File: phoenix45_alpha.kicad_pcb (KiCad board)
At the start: 2 copper layers, 247.7 x 77.5 mm, 114 parts, among them SW1 SW_PUSH, SW2 SW_PUSH, U1 SRV05-4, U3 ATmega32U4-M, X1 Crystal_GND24_Small

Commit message: v1
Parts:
- U3: footprint Package_DFN_QFN:QFN-44-1EP_7x7mm_P0.5mm_EP5.2x5.2mm -> Package_DFN_QFN:QFN-44-1EP_7x7mm_P0.5mm_EP5.2x5.2mm_ThermalVias
- moved D_SPACE13 181.4 mm to (266.6, 38.1), turned to 90 degrees
- moved D_SPACE26 176.1 mm to (266.6, 57.1), turned to 90 degrees
- moved D_SPACE12 147.9 mm to (247.6, 38.1), turned to 90 degrees
- moved D_SPACE47 139.6 mm to (240.4, 95.2), turned to 90 degrees
- moved D_SPACE25 139.5 mm to (247.6, 57.1), turned to 90 degrees
- moved D_SPACE10 137.1 mm to (209.5, 38.1), turned to 90 degrees
- moved D_SPACE1 135.6 mm to (38.0, 38.1), turned to 90 degrees
- moved D_SPACE39 130.1 mm to (261.8, 76.2), turned to 90 degrees
- moved D_SPACE38 127.7 mm to (238.1, 76.2), turned to 90 degrees
- moved D_SPACE11 126.6 mm to (228.5, 38.1), turned to 90 degrees
- moved D_SPACE37 122.8 mm to (219.0, 76.2), turned to 90 degrees
- moved D_SPACE9 119.2 mm to (190.4, 38.1), turned to 90 degrees
- moved D_SPACE2 118.3 mm to (57.1, 38.1), turned to 90 degrees
- moved D_SPACE24 116.1 mm to (228.5, 57.1), turned to 90 degrees
- moved D_SPACE3 114.6 mm to (76.1, 38.1), turned to 90 degrees
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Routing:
- net row0: track 0.00 -> 260.0 mm, vias 0 -> 2
- net row2: track 0.00 -> 254.7 mm
- net row1: track 0.00 -> 237.3 mm, vias 0 -> 3
- net row3: track 0.00 -> 236.3 mm, vias 0 -> 2
- net col0: track 0.00 -> 164.7 mm
- net col12: track 0.00 -> 163.3 mm
- net col1: track 0.00 -> 160.6 mm
- net +5V: track 0.00 -> 159.3 mm, vias 0 -> 7
- net col11: track 0.00 -> 157.7 mm
- net col2: track 0.00 -> 141.1 mm
- net col10: track 0.00 -> 133.7 mm
- net col3: track 0.00 -> 123.6 mm
- net col9: track 0.00 -> 115.4 mm
- net D-: track 0.00 -> 114.5 mm
- net D+: track 0.00 -> 111.8 mm
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
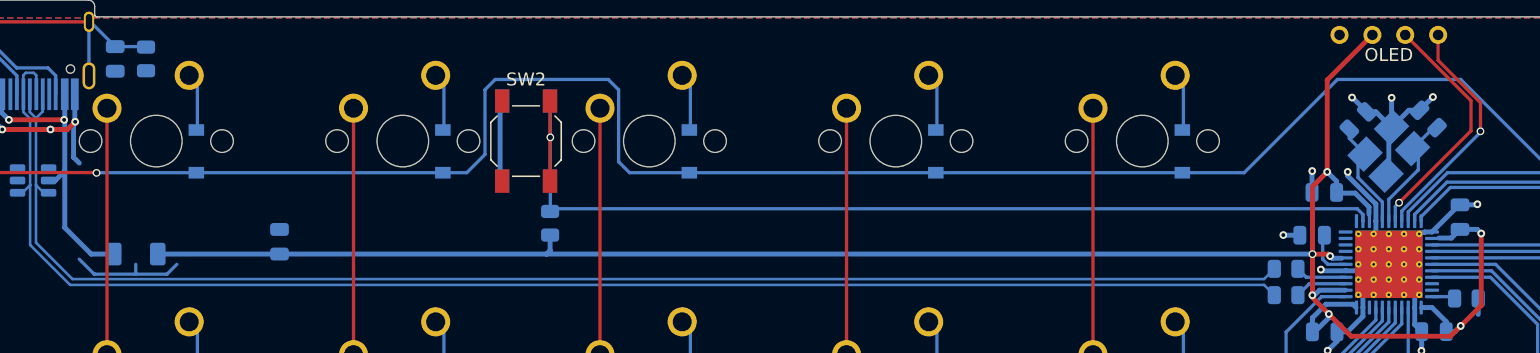
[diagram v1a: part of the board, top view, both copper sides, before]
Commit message: added avr
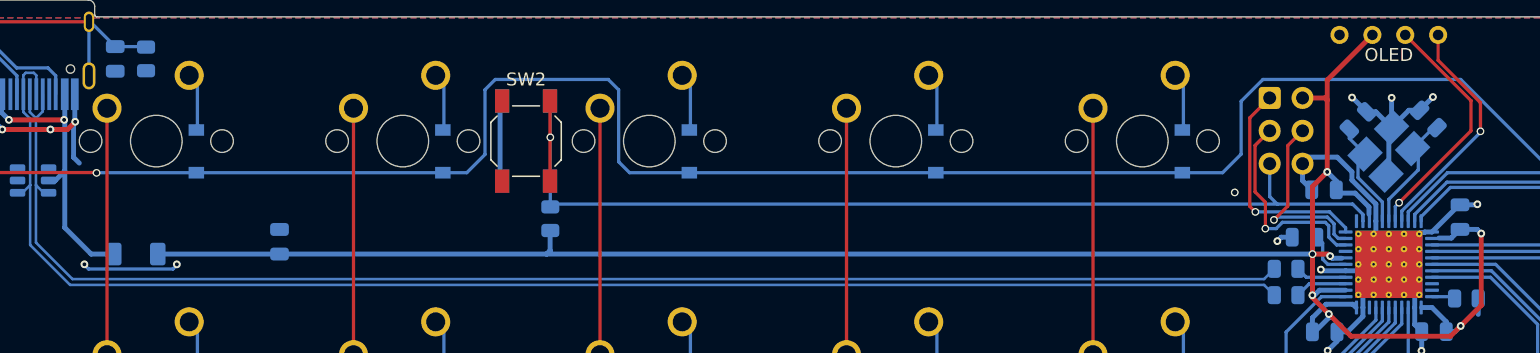
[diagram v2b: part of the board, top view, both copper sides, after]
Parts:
- added J1: AVR-ISP-6, Connector_IDC:IDC-Header_2x03_P2.54mm_Vertical, F.Cu at (140.0, 34.0)
- moved C6 0.61 mm to (142.7, 44.7)
- moved R1 0.35 mm to (84.4, 43.3)
- moved C5 0.20 mm to (144.2, 41.1)
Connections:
- U3 pad 10: unconnected-(U3-Pad10) -> MOSI
- U3 pad 11: unconnected-(U3-Pad11) -> MISO
- U3 pad 9: unconnected-(U3-Pad9) -> SCK
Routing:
- net MISO: track 0.00 -> 17.4 mm, vias 0 -> 1
- net SCK: track 0.00 -> 16.0 mm, vias 0 -> 1
- net MOSI: track 0.00 -> 14.6 mm, vias 0 -> 1
- net GND: track 79.5 -> 83.0 mm, vias 13 -> 14
- net RST: track 77.9 -> 81.0 mm
- net row0: track 260.0 -> 262.5 mm
- net +5V: track 159.3 -> 161.3 mm

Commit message: trackpoint
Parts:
- added C9: 2.2uF, Capacitor_SMD:C_0805_2012Metric_Pad1.18x1.45mm_HandSolder, B.Cu at (164.1, 40.1)
- added TP1: TPCLK, TestPoint:TestPoint_Pad_1.0x1.0mm, B.Cu at (162.6, 44.0)
- added TP2: TPVCC, TestPoint:TestPoint_Pad_1.0x1.0mm, B.Cu at (157.8, 44.0)
- added TP3: TPGND, TestPoint:TestPoint_Pad_1.0x1.0mm, B.Cu at (160.2, 44.0)
- added TP4: TPDATA, TestPoint:TestPoint_Pad_1.0x1.0mm, B.Cu at (167.3, 44.0)
- added TP5: TPRST, TestPoint:TestPoint_Pad_1.0x1.0mm, B.Cu at (165.0, 44.0)
- added UR6: 4.7k, Resistor_SMD:R_0805_2012Metric_Pad1.20x1.40mm_HandSolder, B.Cu at (160.6, 41.0)
- added UR7: 4.7k, Resistor_SMD:R_0805_2012Metric_Pad1.20x1.40mm_HandSolder, B.Cu at (157.7, 41.0)
- added UR8: 100k, Resistor_SMD:R_0805_2012Metric_Pad1.20x1.40mm_HandSolder, B.Cu at (164.1, 42.1)
- C0, C1, C2, C3, C4, C5, C6, C7, C8: footprint Capacitor_SMD:C_0805_2012Metric -> Capacitor_SMD:C_0805_2012Metric_Pad1.18x1.45mm_HandSolder
- R1, R2, UR1, UR2, UR3, UR4, UR5: footprint Resistor_SMD:R_0805_2012Metric -> Resistor_SMD:R_0805_2012Metric_Pad1.20x1.40mm_HandSolder
- U1: footprint Package_TO_SOT_SMD:SOT-23-6 -> Package_TO_SOT_SMD:SOT-23-6_Handsoldering
- moved R2 0.56 mm to (155.4, 50.0)
- moved C6 0.24 mm to (142.5, 44.7)
- moved R1 0.18 mm to (84.4, 43.5)
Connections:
- U3 pad 20: row0 -> PD2
- U3 pad 21: col12 -> row0
- U3 pad 22: col11 -> PD5
- U3 pad 25: col10 -> col12
- U3 pad 26: col9 -> col11
- U3 pad 27: col8 -> col10
- U3 pad 28: col7 -> col9
- U3 pad 29: row2 -> col8
- U3 pad 30: row3 -> col7
- U3 pad 31: encA -> row2
- U3 pad 32: encB -> row3
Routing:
- net PD2: track 0.00 -> 21.8 mm, vias 0 -> 2
- net +5V: track 161.3 -> 174.8 mm, vias 7 -> 9
- net PD5: track 0.00 -> 13.1 mm
- net GND: track 83.0 -> 88.7 mm, vias 14 -> 18
- net col12: track 163.3 -> 158.4 mm
- net col11: track 157.7 -> 153.5 mm
- net Net-(C9-Pad2): track 0.00 -> 3.74 mm
- net row0: track 262.5 -> 264.7 mm
- net MOSI: track 14.6 -> 15.5 mm
- net Net-(C8-Pad1): track 7.84 -> 7.14 mm
- net Net-(R2-Pad2): track 1.61 -> 2.15 mm

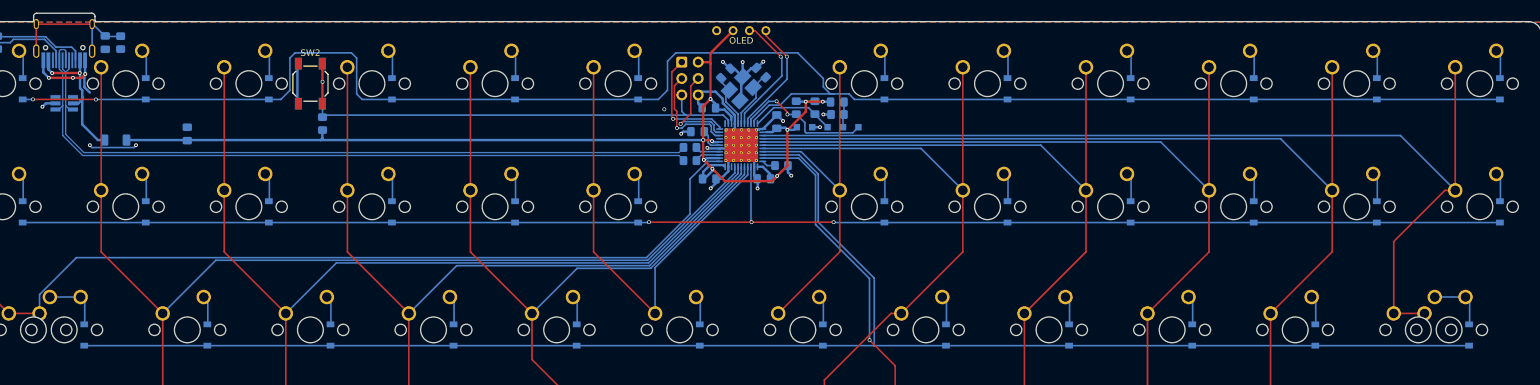
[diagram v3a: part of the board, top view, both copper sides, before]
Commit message: qfn + tqfp
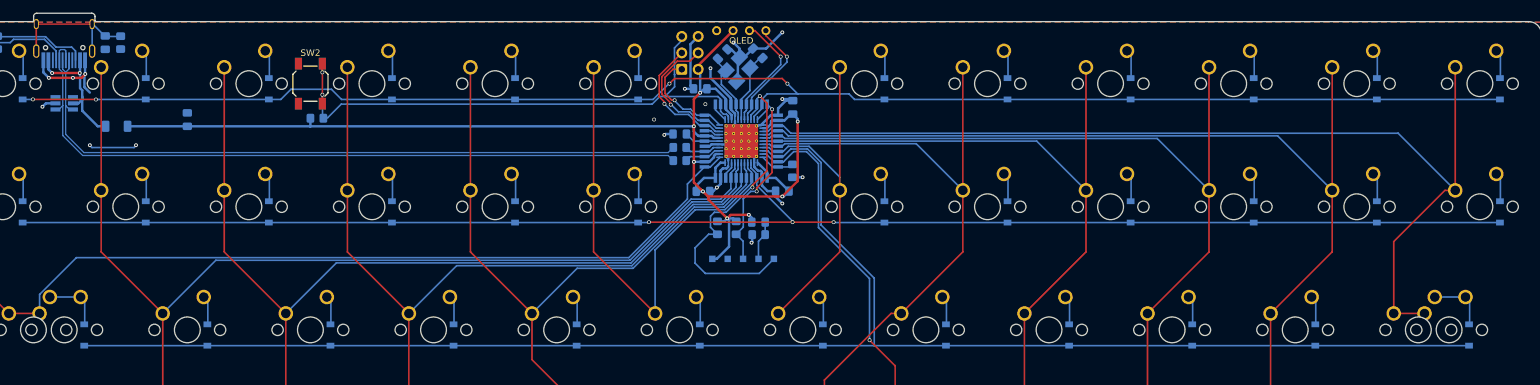
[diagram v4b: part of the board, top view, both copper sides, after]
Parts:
- added U2: ATmega32U4-M, Package_DFN_QFN:QFN-44-1EP_7x7mm_P0.5mm_EP5.2x5.2mm_ThermalVias, B.Cu at (149.2, 46.2)
- J1: moved to B.Cu
- U3: footprint Package_DFN_QFN:QFN-44-1EP_7x7mm_P0.5mm_EP5.2x5.2mm_ThermalVias -> Package_QFP:TQFP-44_10x10mm_P0.8mm
- moved TP1 24.2 mm to (149.5, 64.4)
- moved TP4 24.2 mm to (154.3, 64.4)
- moved TP5 24.2 mm to (151.9, 64.4)
- moved TP2 24.2 mm to (144.7, 64.4)
- moved TP3 24.2 mm to (147.1, 64.4)
- moved UR8 22.2 mm to (151.9, 60.7)
- moved C9 22.2 mm to (151.9, 58.7)
- moved UR6 22.2 mm to (148.4, 59.6)
- moved UR7 22.2 mm to (145.5, 59.6)
- moved C3 3.44 mm to (155.6, 53.9)
- moved C4 3.31 mm to (157.2, 41.0)
- moved C5 3.26 mm to (142.9, 38.1)
- moved C7 3.03 mm to (151.8, 32.6)
- moved C8 3.03 mm to (146.3, 32.7)
- moved X1 3.03 mm to (148.7, 35.1)
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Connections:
- U3 pad 12: unconnected-(U3-Pad12) -> Net-(U3-Pad12)
- U3 pad 42: unconnected-(U3-Pad42) -> Net-(U3-Pad42)
- U3 pad 8: unconnected-(U3-Pad8) -> Net-(U3-Pad8)
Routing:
- net +5V: track 174.8 -> 204.8 mm, vias 9 -> 8
- net PD2: track 21.8 -> 51.8 mm
- net row0: track 264.7 -> 242.2 mm, vias 2 -> 4
- net PD5: track 13.1 -> 30.5 mm, vias 0 -> 2
- net GND: track 88.7 -> 100.2 mm
- net RST: track 81.0 -> 87.5 mm, vias 1 -> 2
- net MOSI: track 15.5 -> 21.1 mm
- net col5: track 70.7 -> 74.5 mm
- net Net-(C8-Pad1): track 7.14 -> 10.7 mm
- net SCK: track 16.4 -> 20.0 mm
- net row1: track 237.3 -> 240.5 mm
- net Net-(U3-Pad12): track 0.00 -> 2.98 mm
- net row3: track 235.9 -> 238.8 mm
- net Net-(U3-Pad42): track 0.00 -> 2.74 mm
- net Net-(R2-Pad2): track 2.15 -> 4.83 mm
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
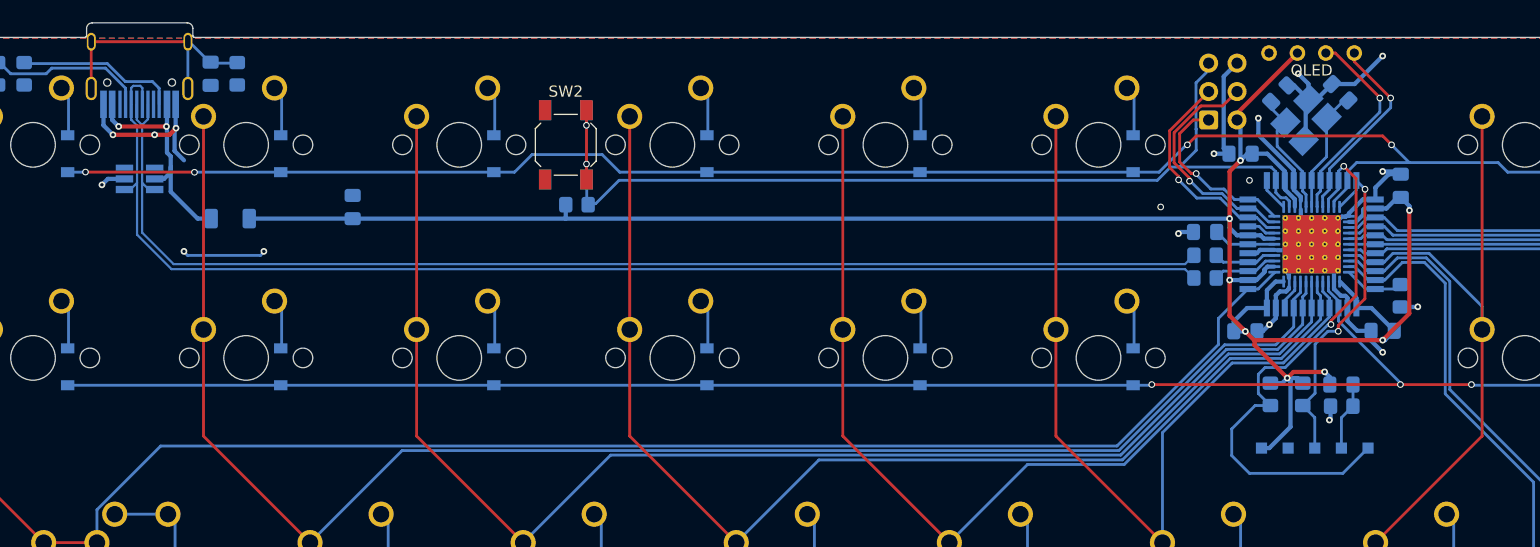
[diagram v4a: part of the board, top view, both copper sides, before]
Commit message: Move TP connectors to front
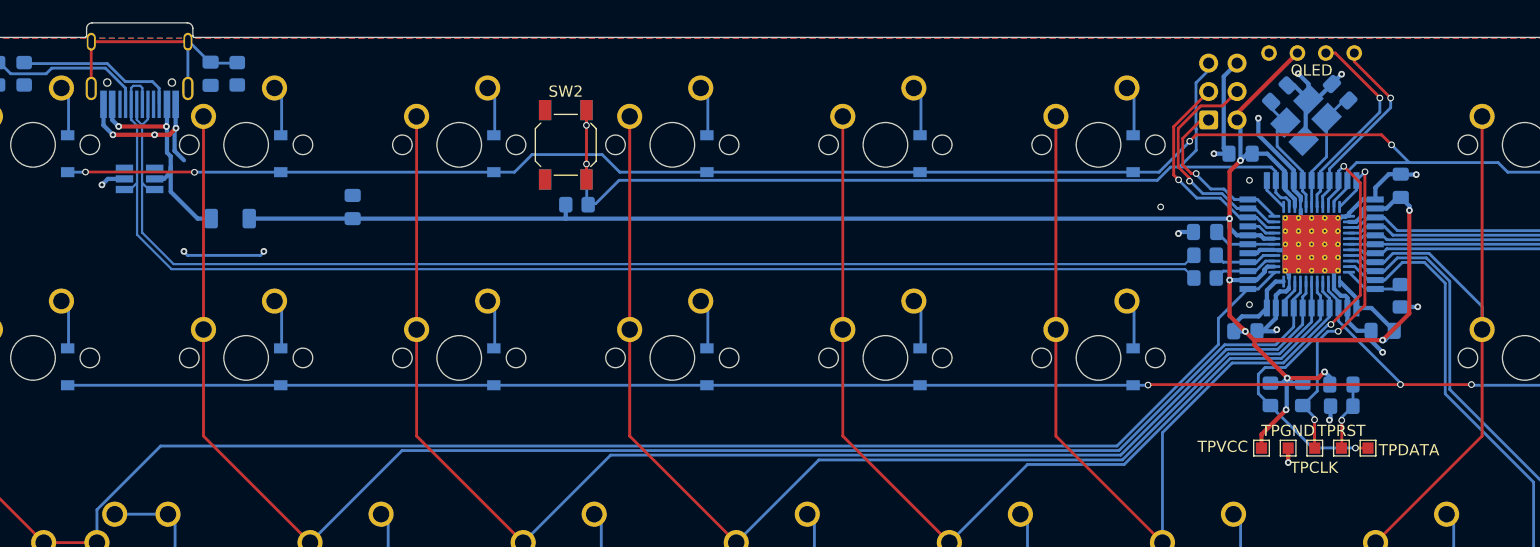
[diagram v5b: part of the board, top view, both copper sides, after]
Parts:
- TP1, TP2, TP3, TP4, TP5: moved to F.Cu
- turned TP1 to 180 degrees
- turned TP2 to 180 degrees
- turned TP3 to 180 degrees
- turned TP4 to 180 degrees
- turned TP5 to 180 degrees
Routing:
- net PD2: track 51.8 -> 42.0 mm, vias 2 -> 3
- net PD5: track 30.5 -> 32.1 mm, vias 2 -> 3
- net GND: track 100.2 -> 99.0 mm, vias 18 -> 20
- net +5V: track 204.8 -> 204.0 mm, vias 8 -> 9
- net MISO: track 16.1 -> 15.5 mm
- net Net-(C9-Pad2): track 6.10 -> 6.11 mm, vias 0 -> 1

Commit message: THT
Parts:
- C9: footprint Capacitor_SMD:C_0805_2012Metric_Pad1.18x1.45mm_HandSolder -> Capacitor_THT:CP_Radial_D4.0mm_P1.50mm; moved to F.Cu
- UR6, UR7, UR8: footprint Resistor_SMD:R_0805_2012Metric_Pad1.20x1.40mm_HandSolder -> Resistor_THT:R_Axial_DIN0207_L6.3mm_D2.5mm_P7.62mm_Horizontal; moved to F.Cu
- moved UR7 12.5 mm to (158.0, 59.4), turned to 180 degrees
- moved C9 5.03 mm to (147.8, 61.7), turned to -90 degrees
- moved UR8 2.35 mm to (150.4, 62.5), turned to 0 degrees
- moved TP1 0.83 mm to (149.1, 65.1)
- moved TP2 0.83 mm to (144.3, 65.1)
- moved TP3 0.83 mm to (146.7, 65.1)
- moved TP5 0.83 mm to (151.5, 65.1)
- moved TP4 0.83 mm to (153.8, 65.1)
- moved UR6 0.61 mm to (147.9, 59.4), turned to 180 degrees
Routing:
- net PD5: track 32.1 -> 43.7 mm
- net row1: track 240.5 -> 246.2 mm
- net PD2: track 42.0 -> 38.0 mm, vias 3 -> 2
- net +5V: track 204.0 -> 200.4 mm, vias 9 -> 7
- net GND: track 99.0 -> 96.1 mm, vias 20 -> 18
- net col0: track 163.2 -> 162.4 mm
- net col5: track 74.5 -> 75.3 mm
- net MISO: track 15.5 -> 14.8 mm
- net Net-(TP5-Pad1): track 6.11 -> 6.42 mm, vias 1 -> 0
